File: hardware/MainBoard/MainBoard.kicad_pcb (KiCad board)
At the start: 2 copper layers, 50 x 80 mm, 31 parts, among them J101 Servo, J102 Relay, J103 MotorDriver, J104 MPU9250, J105 PicoBATT+, J106 Tachometer, J201 Micro_SD_Card, SW101 Reset, SW102 SW_Pico, SW103 SW_BATT

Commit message: シルクをしてみた
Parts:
- moved D101 1.05 mm to (159.2, 86.1)
- moved D103 1.05 mm to (159.2, 81.6)
- moved D102 1.03 mm to (159.2, 77.1)
- moved R101 0.50 mm to (154.5, 86.6)
- moved R103 0.50 mm to (156.7, 81.6)
- moved J105 0.40 mm to (154.5, 48.4)
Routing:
- net /Relay_S: track 57.0 -> 55.9 mm
- net /ERROR: track 42.5 -> 41.4 mm
- net Net-(D102-K): track 7.75 -> 6.72 mm
- net VDD: track 188.6 -> 187.8 mm
- net Net-(A101-3V3_EN): track 24.7 -> 23.9 mm
- net Net-(D103-K): track 3.03 -> 2.50 mm
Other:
- board text added: "ERROR"
- board text added: "GND"
- board text added: "IN1"
- board text added: "IN2"
- board text added: "IN3"
- board text added: "IN4"
- board text added: "MotorDriver"
- board text added: "OUT1"
- board text added: "OUT2"
- board text added: "Pico_BATT"
- board text added: "Relay"
- board text added: "Reset"
- board text added: "S"
- board text added: "STAT"
- board text added: "SW_BATT"
- board text added: "SW_Pico"
- board text added: "Servo"
- board text added: "Tachometer"
- board text added: "VDD"

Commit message: ちょっとシルク変更してスイッチ追加
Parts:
- removed REF** (x2): MountingHole_3.2mm_M3, MountingHole:MountingHole_3.2mm_M3
- added J202: Stop, Connector_JST:JST_PH_B2B-PH-K_1x02_P2.00mm_Vertical, F.Cu at (125.0, 41.5)
- added R205: 10k, Resistor_THT:R_Axial_DIN0204_L3.6mm_D1.6mm_P5.08mm_Horizontal, F.Cu at (124.6, 30.4)
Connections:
- A101 pad 2: unconnected-(A101-GPIO1-Pad2) -> Net-(A101-GPIO1)
- SW102 pad 1: Net-(A101-3V3_EN) -> unconnected-(SW102-A-Pad1)
- SW102 pad 3: unconnected-(SW102-C-Pad3) -> Net-(A101-3V3_EN)
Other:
- board text added: "LiPo"
- board text added: "Main"
- board text added: "OFF"
- board text added: "ON"
- board text added: "VPP"
- board text removed: "Pico_BATT"
- board text removed: "SW_Pico"

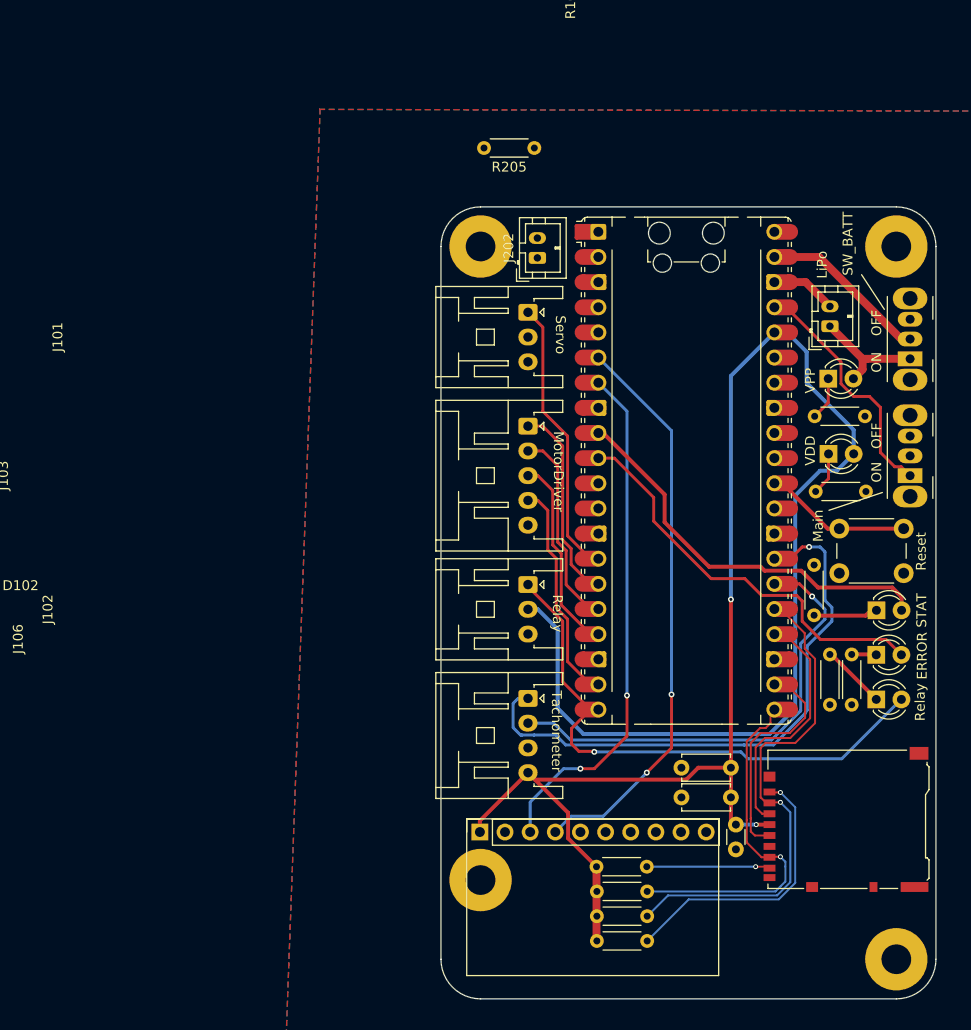
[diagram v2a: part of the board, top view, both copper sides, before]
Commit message: シルク追加してちょっと配線変更
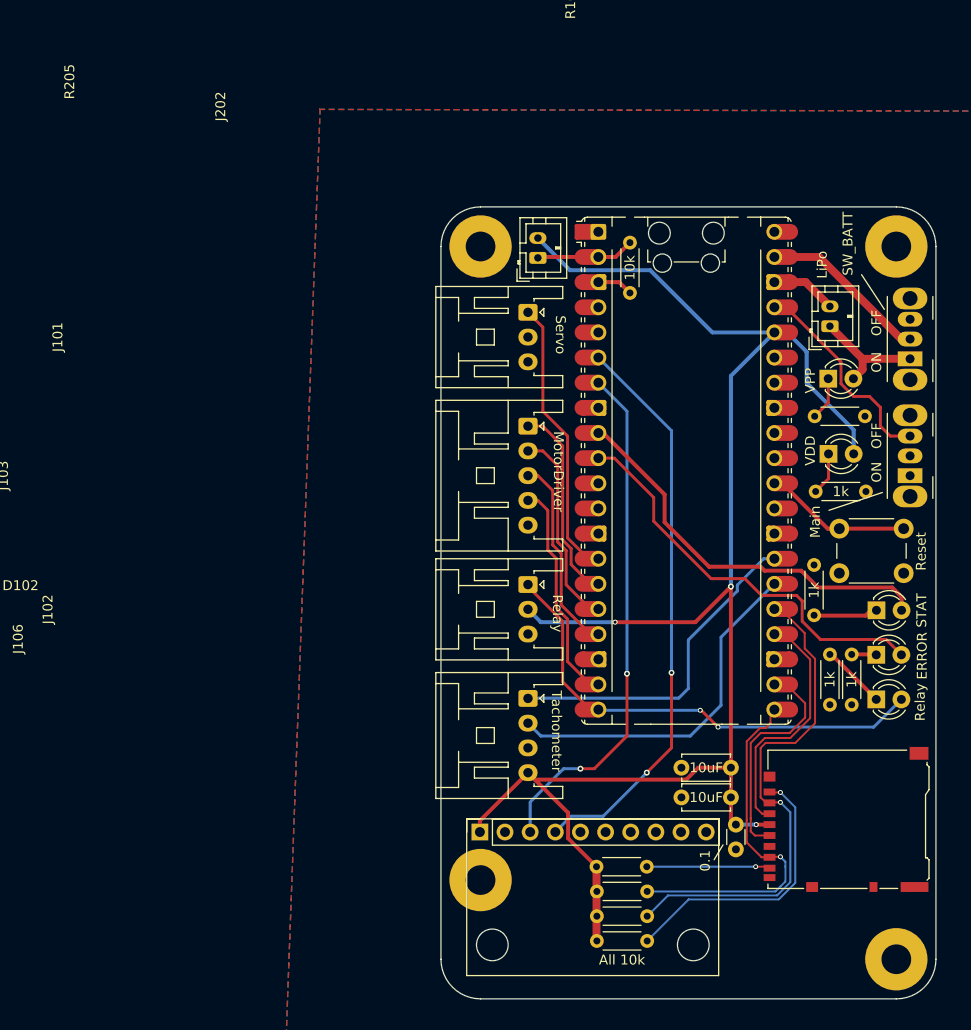
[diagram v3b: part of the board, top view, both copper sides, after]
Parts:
- added ?: , , F.Cu at (140.7, 110.9)
- added REF**: MountingHole_3.2mm_M3_DIN965, MountingHole:MountingHole_3.2mm_M3_DIN965, F.Cu at (120.4, 110.9)
- C203: value 0.1uF -> 0.1
- R204: value 10k -> All 10k
- moved R205 13.6 mm to (134.3, 40.0), turned to -90 degrees
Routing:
- net /OUT2: track 58.4 -> 34.0 mm, vias 1 -> 0
- net VDD: track 187.8 -> 171.0 mm, vias 2 -> 3
- net /OUT1: track 46.1 -> 35.8 mm, vias 1 -> 0
- net Net-(A101-GPIO1): track 0.00 -> 9.14 mm
- net /Relay_S: track 55.9 -> 47.7 mm, vias 1 -> 2
- net GND: track 5.82 -> 9.47 mm
- net Net-(A101-3V3_EN): track 23.9 -> 20.7 mm

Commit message: もう一回
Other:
- board text added: "GND/IN4/3/2/1"
- board text added: "GND/VDD/SIG"
- board text added: "GND/X/SIG"
- board text added: "VDD/GND/OUT1/2"
- board text removed: "GND"
- board text removed: "IN1"
- board text removed: "IN2"
- board text removed: "IN3"
- board text removed: "IN4"
- board text removed: "OUT1"
- board text removed: "OUT2"
- board text removed: "S"
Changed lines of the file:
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@@
 		)
 	)
-	(gr_text "GND"
-		(at 126.3 53.8 270)
+	(gr_text "GND/X/SIG"
+		(at 125.9 53.6 270)
 		(layer "B.SilkS")
 		(effects
@@
 		)
 	)
-	(gr_text "IN1"
-		(at 126.2 59.35 270)
+	(gr_text "GND/IN4/3/2/1"
+		(at 126 69.5 270)
 		(layer "B.SilkS")
 		(effects
@@
 		)
 	)
-	(gr_text "GND"
-		(at 126.2 70.4 270)
+	(gr_text "GND/VDD/SIG"
+		(at 126 82 270)
 		(layer "B.SilkS")
 		(effects
@@
 		)
 	)
-	(gr_text "IN2"
-		(at 126.25 62 270)
+	(gr_text "Relay"
+		(at 120.8 79 270)
 		(layer "B.SilkS")
 		(effects
@@
 		)
 	)
-	(gr_text "VDD"
-		(at 126.15 77.6 270)
+	(gr_text "MotorDriver"
+		(at 120.8 67.6 270)
 		(layer "B.SilkS")
 		(effects
@@
 		)
 	)
-	(gr_text "GND"
-		(at 126.15 81.1 270)
+	(gr_text "VDD/GND/OUT1/2"
+		(at 126 96.7 270)
 		(layer "B.SilkS")
 		(effects
@@
 		)
 	)
-	(gr_text "GND"
-		(at 126.45 93.1 270)
+	(gr_text "Servo"
+		(at 120.8 51.6 270)
 		(layer "B.SilkS")
 		(effects
@@
 		)
 	)
-	(gr_text "IN4"
-		(at 126.25 67.25 270)
+	(gr_text "Tachometer"
+		(at 120.8 93.7 270)
 		(layer "B.SilkS")
 		(effects
-			(font
-				(size 1 1)
-				(thickness 0.1)
-			)
-			(justify left bottom mirror)
-		)
-	)
-	(gr_text "S"
-		(at 126.3 47.65 270)
-		(layer "B.SilkS")
-		(effects
-			(font
-				(size 1 1)
-				(thickness 0.1)
-			)
-			(justify left bottom mirror)
-		)
-	)
-	(gr_text "S"
-		(at 126.15 74.45 270)
-		(layer "B.SilkS")
-		(effects
-			(font
-				(size 1 1)
-				(thickness 0.1)
-			)
-			(justify left bottom mirror)
-		)
-	)
-	(gr_text "VDD"
-		(at 125.3 95.3 270)
-		(layer "B.SilkS")
-		(effects
-			(font
-				(size 1 1)
-				(thickness 0.1)
-			)
-			(justify left bottom mirror)
-		)
-	)
-	(gr_text "IN3"
-		(at 126.25 64.7 270)
-		(layer "B.SilkS")
-		(effects
-			(font
-				(size 1 1)
-				(thickness 0.1)
-			)
-			(justify left bottom mirror)
-		)
-	)
-	(gr_text "OUT1"
-		(at 125.1 90.8 270)
-		(layer "B.SilkS")
-		(effects
-			(font
-				(size 1 1)
-				(thickness 0.1)
-			)
-			(justify left bottom mirror)
-		)
-	)
-	(gr_text "OUT2"
-		(at 126.3 87.75 270)
-		(layer "B.SilkS")
-		(effects
